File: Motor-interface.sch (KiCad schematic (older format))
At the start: 40 parts, among them J101 0, J102 0, P101 TE-23pins connector, P102 PSU_ISO, P103 Halls, P104 LineContactor, P105 ReverseContactor, P106 FanContactor, P107 Battery+, P108 MC_USB, P109 MC_CAN, P110 HallCurrent, Q101 Q_NPN_BCE, U101 AP1117D50, U102 AP1117D33, U103 TLP2361, U104 TLP2361, U105 TLP2361, U106 TLP2361, U107 TLP2361, U108 TLP2361, U109 Teensy_3.2, U110 TLP2361, U111 FODM3052

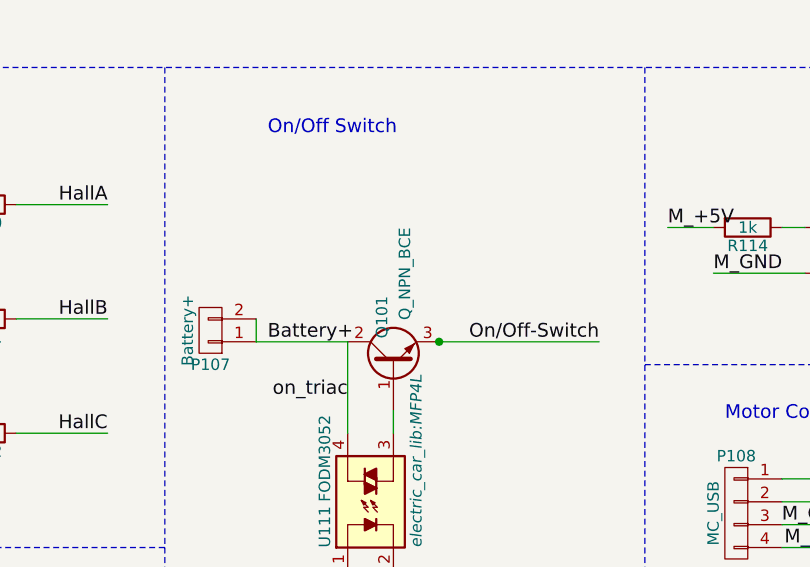
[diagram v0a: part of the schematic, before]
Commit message: renamed transistor (fixed)
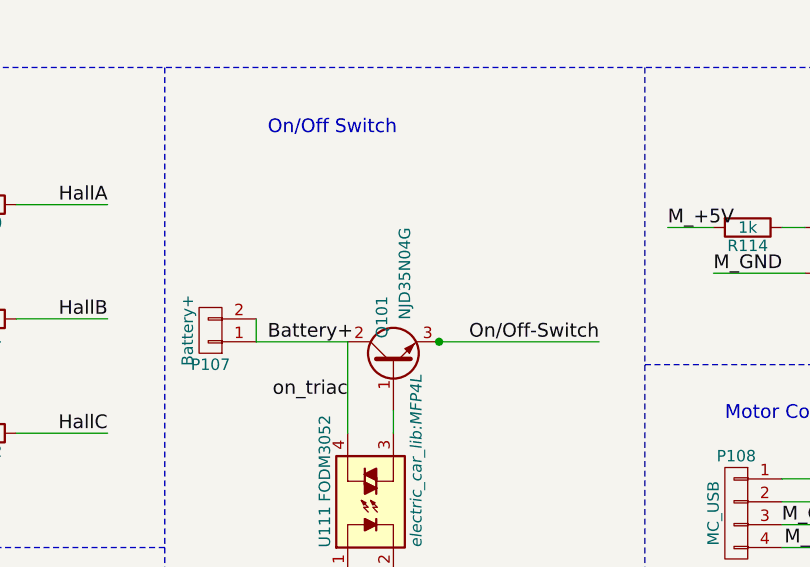
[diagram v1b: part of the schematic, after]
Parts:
- Q101: value Q_NPN_BCE -> NJD35N04G
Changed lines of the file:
@@
 P 7700 4500
 F 0 "Q101" H 8000 4550 50  0000 R CNN
-F 1 "Q_NPN_BCE" H 8300 4450 50  0000 R CNN
+F 1 "NJD35N04G" H 8300 4450 50  0000 R CNN
 F 2 "TO_SOT_Packages_SMD:SOT-428" H 7900 4600 50  0001 C CNN
 F 3 "" H 7700 4500 50  0000 C CNN

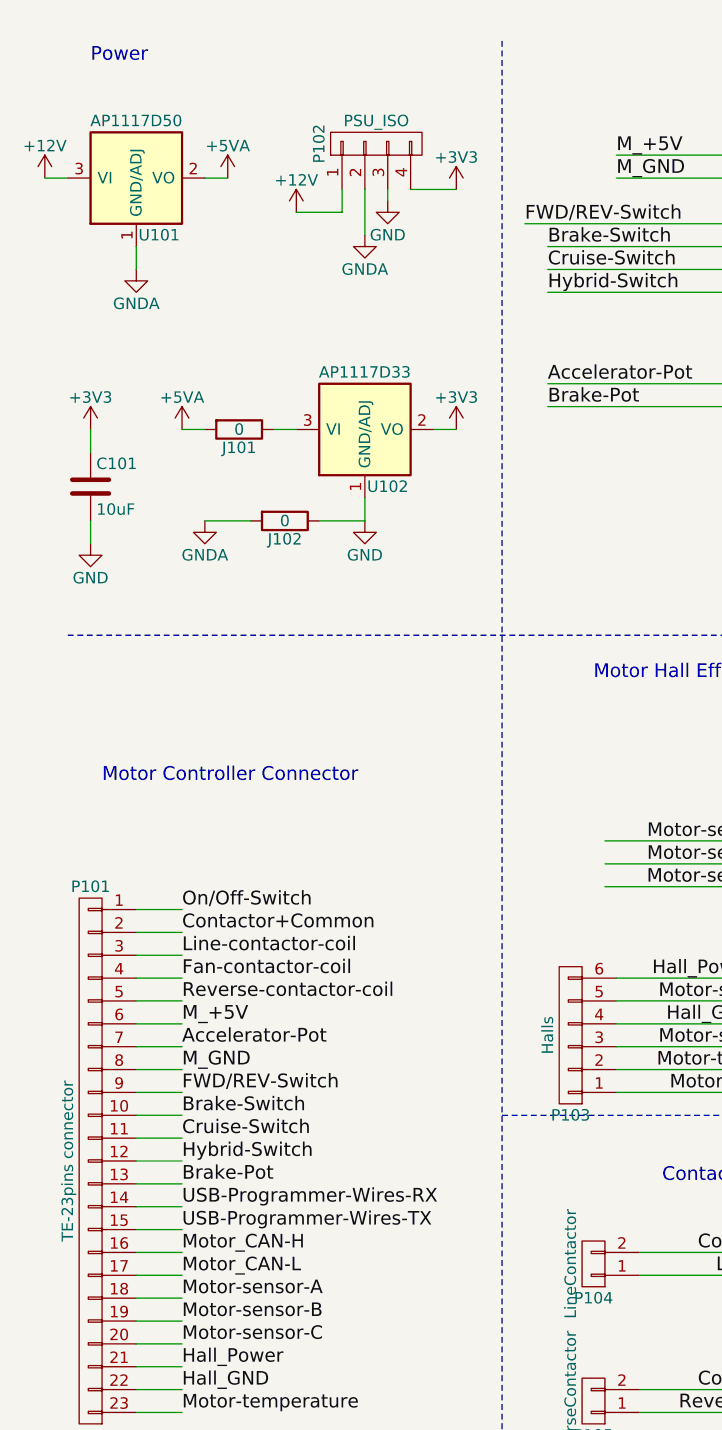
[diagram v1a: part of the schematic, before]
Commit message: pour and silk edits
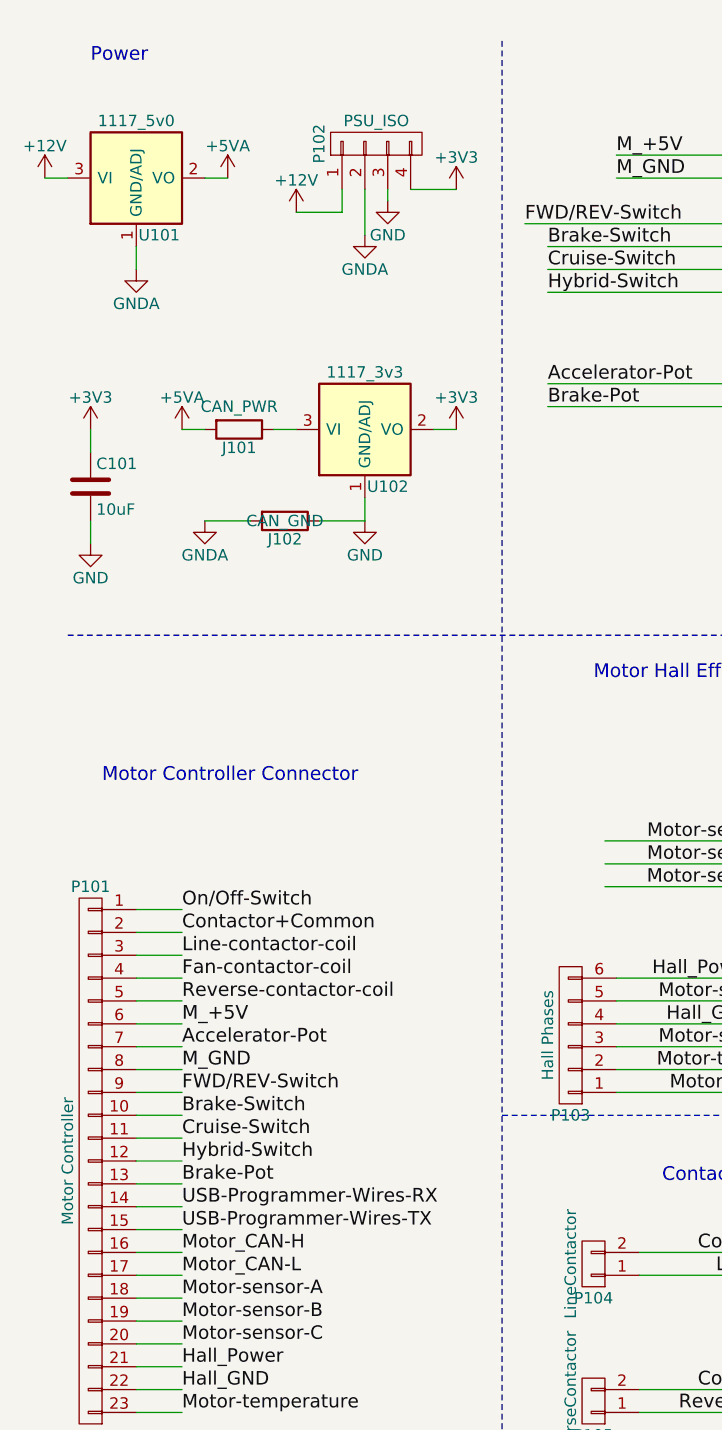
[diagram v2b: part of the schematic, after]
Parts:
- J101: value 0 -> CAN_PWR
- J102: value 0 -> CAN_GND
- P101: value TE-23pins connector -> Motor Controller
- P103: value Halls -> Hall Phases
- U101: value AP1117D50 -> 1117_5v0
- U102: value AP1117D33 -> 1117_3v3
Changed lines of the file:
@@
 P 800 5500
 F 0 "P101" H 800 6700 50  0000 C CNN
-F 1 "TE-23pins connector" V 900 5500 50  0000 C CNN
+F 1 "Motor Controller" V 900 5500 50  0000 C CNN
 F 2 "electric_car_lib:TE_23_pins_776087-1_connector" H 800 5500 50  0001 C CNN
 F 3 "" H 800 5500 50  0000 C CNN
@@
 P 2900 4950
 F 0 "P103" H 2900 5300 50  0000 C CNN
-F 1 "Halls" V 3000 4950 50  0000 C CNN
+F 1 "Hall Phases" V 3000 4950 50  0000 C CNN
 F 2 "Pin_Headers:Pin_Header_Angled_2x03" H 2900 4950 50  0001 C CNN
 F 3 "" H 2900 4950 50  0000 C CNN
@@
 P 2000 2300
 F 0 "U102" H 2100 2050 50  0000 C CNN
-F 1 "AP1117D33" H 2000 2550 50  0000 C CNN
+F 1 "1117_3v3" H 2000 2550 50  0000 C CNN
 F 2 "TO_SOT_Packages_SMD:SOT-223" H 2000 2300 50  0001 C CNN
 F 3 "" H 2000 2300 50  0000 C CNN
@@
 P 1000 1200
 F 0 "U101" H 1100 950 50  0000 C CNN
-F 1 "AP1117D50" H 1000 1450 50  0000 C CNN
+F 1 "1117_5v0" H 1000 1450 50  0000 C CNN
 F 2 "TO_SOT_Packages_SMD:SOT-223" H 1000 1200 50  0001 C CNN
 F 3 "" H 1000 1200 50  0000 C CNN
@@
 P 1650 2700
 F 0 "J102" V 1730 2700 50  0000 C CNN
-F 1 "0" V 1650 2700 50  0000 C CNN
+F 1 "CAN_GND" V 1650 2700 50  0000 C CNN
 F 2 "Resistors_SMD:R_1210_HandSoldering" V 1580 2700 50  0001 C CNN
 F 3 "" H 1650 2700 50  0000 C CNN
@@
 P 1450 2300
 F 0 "J101" V 1530 2300 50  0000 C CNN
-F 1 "0" V 1450 2300 50  0000 C CNN
+F 1 "CAN_PWR" V 1350 2300 50  0000 C CNN
 F 2 "Resistors_SMD:R_1210_HandSoldering" V 1380 2300 50  0001 C CNN
 F 3 "" H 1450 2300 50  0000 C CNN

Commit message: plotted gerbers
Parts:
- added W101, W102: M3, Mounting_Holes:MountingHole_3.5mm_Pad_Via, symbol TEST_1P
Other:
- note added: "Mounting Holes"
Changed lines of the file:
@@
 MOSI
 $Comp
-L GND #PWR01
+L GND #PWR129
 U 1 1 57FCC1C9
 P 7700 5500
-F 0 "#PWR01" H 7700 5250 50  0001 C CNN
+F 0 "#PWR129" H 7700 5250 50  0001 C CNN
 F 1 "GND" H 7700 5350 50  0000 C CNN
 F 2 "" H 7700 5500 50  0000 C CNN
@@
 Motor_CAN-L
 $Comp
-L +3V3 #PWR02
+L +3V3 #PWR128
 U 1 1 582A5D02
 P 7050 1400
-F 0 "#PWR02" H 7050 1250 50  0001 C CNN
+F 0 "#PWR128" H 7050 1250 50  0001 C CNN
 F 1 "+3V3" H 7050 1540 50  0000 C CNN
 F 2 "" H 7050 1400 50  0000 C CNN
@@
 $EndComp
 $Comp
-L GND #PWR03
+L GND #PWR130
 U 1 1 582A5FC1
 P 8850 1200
-F 0 "#PWR03" H 8850 950 50  0001 C CNN
+F 0 "#PWR130" H 8850 950 50  0001 C CNN
 F 1 "GND" H 8850 1050 50  0000 C CNN
 F 2 "" H 8850 1200 50  0000 C CNN
@@
 $EndComp
 $Comp
-L +3V3 #PWR04
+L +3V3 #PWR117
 U 1 1 582BF0B6
 P 5700 5900
-F 0 "#PWR04" H 5700 5750 50  0001 C CNN
+F 0 "#PWR117" H 5700 5750 50  0001 C CNN
 F 1 "+3V3" H 5700 6040 50  0000 C CNN
 F 2 "" H 5700 5900 50  0000 C CNN
@@
 $EndComp
 $Comp
-L +3V3 #PWR05
+L +3V3 #PWR119
 U 1 1 582BF605
 P 5700 6500
-F 0 "#PWR05" H 5700 6350 50  0001 C CNN
+F 0 "#PWR119" H 5700 6350 50  0001 C CNN
 F 1 "+3V3" H 5700 6640 50  0000 C CNN
 F 2 "" H 5700 6500 50  0000 C CNN
@@
 $EndComp
 $Comp
-L +3V3 #PWR06
+L +3V3 #PWR121
 U 1 1 582BF6C1
 P 5700 7100
-F 0 "#PWR06" H 5700 6950 50  0001 C CNN
+F 0 "#PWR121" H 5700 6950 50  0001 C CNN
 F 1 "+3V3" H 5700 7240 50  0000 C CNN
 F 2 "" H 5700 7100 50  0000 C CNN
@@
 $EndComp
 $Comp
-L GND #PWR07
+L GND #PWR118
 U 1 1 582BF99C
 P 5700 6100
-F 0 "#PWR07" H 5700 5850 50  0001 C CNN
+F 0 "#PWR118" H 5700 5850 50  0001 C CNN
 F 1 "GND" H 5700 5950 50  0000 C CNN
 F 2 "" H 5700 6100 50  0000 C CNN
@@
 $EndComp
 $Comp
-L GND #PWR08
+L GND #PWR120
 U 1 1 582BFB0B
 P 5700 6700
-F 0 "#PWR08" H 5700 6450 50  0001 C CNN
+F 0 "#PWR120" H 5700 6450 50  0001 C CNN
 F 1 "GND" H 5700 6550 50  0000 C CNN
 F 2 "" H 5700 6700 50  0000 C CNN
@@
 $EndComp
 $Comp
-L GND #PWR09
+L GND #PWR122
 U 1 1 582BFBC7
 P 5700 7300
-F 0 "#PWR09" H 5700 7050 50  0001 C CNN
+F 0 "#PWR122" H 5700 7050 50  0001 C CNN
 F 1 "GND" H 5700 7150 50  0000 C CNN
 F 2 "" H 5700 7300 50  0000 C CNN
@@
 Connection ~ 4450 4200
 $Comp
-L +3V3 #PWR010
+L +3V3 #PWR123
 U 1 1 582D2C82
 P 5850 3700
-F 0 "#PWR010" H 5850 3550 50  0001 C CNN
+F 0 "#PWR123" H 5850 3550 50  0001 C CNN
 F 1 "+3V3" H 5850 3840 50  0000 C CNN
 F 2 "" H 5850 3700 50  0000 C CNN
@@
 $EndComp
 $Comp
-L +3V3 #PWR011
+L +3V3 #PWR124
 U 1 1 582D2E5B
 P 5850 4200
-F 0 "#PWR011" H 5850 4050 50  0001 C CNN
+F 0 "#PWR124" H 5850 4050 50  0001 C CNN
 F 1 "+3V3" H 5850 4340 50  0000 C CNN
 F 2 "" H 5850 4200 50  0000 C CNN
@@
 $EndComp
 $Comp
-L +3V3 #PWR012
+L +3V3 #PWR125
 U 1 1 582D2F32
 P 5850 4700
-F 0 "#PWR012" H 5850 4550 50  0001 C CNN
+F 0 "#PWR125" H 5850 4550 50  0001 C CNN
 F 1 "+3V3" H 5850 4840 50  0000 C CNN
 F 2 "" H 5850 4700 50  0000 C CNN
@@
 $EndComp
 $Comp
-L GND #PWR013
+L GND #PWR114
 U 1 1 582D31E1
 P 5650 3900
-F 0 "#PWR013" H 5650 3650 50  0001 C CNN
+F 0 "#PWR114" H 5650 3650 50  0001 C CNN
 F 1 "GND" H 5650 3750 50  0000 C CNN
 F 2 "" H 5650 3900 50  0000 C CNN
@@
 $EndComp
 $Comp
-L GND #PWR014
+L GND #PWR115
 U 1 1 582D35E6
 P 5650 4400
-F 0 "#PWR014" H 5650 4150 50  0001 C CNN
+F 0 "#PWR115" H 5650 4150 50  0001 C CNN
 F 1 "GND" H 5650 4250 50  0000 C CNN
 F 2 "" H 5650 4400 50  0000 C CNN
@@
 $EndComp
 $Comp
-L GND #PWR015
+L GND #PWR116
 U 1 1 582D36BD
 P 5650 4900
-F 0 "#PWR015" H 5650 4650 50  0001 C CNN
+F 0 "#PWR116" H 5650 4650 50  0001 C CNN
 F 1 "GND" H 5650 4750 50  0000 C CNN
 F 2 "" H 5650 4900 50  0000 C CNN
@@
 	8900 3900 9100 3900
 $Comp
-L +3V3 #PWR016
+L +3V3 #PWR131
 U 1 1 582D6DBE
 P 10200 3900
-F 0 "#PWR016" H 10200 3750 50  0001 C CNN
+F 0 "#PWR131" H 10200 3750 50  0001 C CNN
 F 1 "+3V3" H 10200 4040 50  0000 C CNN
 F 2 "" H 10200 3900 50  0000 C CNN
@@
 $EndComp
 $Comp
-L GND #PWR017
+L GND #PWR132
 U 1 1 582D6EA4
 P 10200 4100
-F 0 "#PWR017" H 10200 3850 50  0001 C CNN
+F 0 "#PWR132" H 10200 3850 50  0001 C CNN
 F 1 "GND" H 10200 3950 50  0000 C CNN
 F 2 "" H 10200 4100 50  0000 C CNN
@@
 	9400 2200 8700 2200
 $Comp
-L +12V #PWR018
+L +12V #PWR101
 U 1 1 582DCA99
 P 600 1200
-F 0 "#PWR018" H 600 1050 50  0001 C CNN
+F 0 "#PWR101" H 600 1050 50  0001 C CNN
 F 1 "+12V" H 600 1340 50  0000 C CNN
 F 2 "" H 600 1200 50  0000 C CNN
@@
 $EndComp
 $Comp
-L +3V3 #PWR019
+L +3V3 #PWR113
 U 1 1 582DCE09
 P 2400 2300
-F 0 "#PWR019" H 2400 2150 50  0001 C CNN
+F 0 "#PWR113" H 2400 2150 50  0001 C CNN
 F 1 "+3V3" H 2400 2440 50  0000 C CNN
 F 2 "" H 2400 2300 50  0000 C CNN
@@
 $EndComp
 $Comp
-L +5VA #PWR020
+L +5VA #PWR107
 U 1 1 582DCF91
 P 1400 1200
-F 0 "#PWR020" H 1400 1050 50  0001 C CNN
+F 0 "#PWR107" H 1400 1050 50  0001 C CNN
 F 1 "+5VA" H 1400 1340 50  0000 C CNN
 F 2 "" H 1400 1200 50  0000 C CNN
@@
 $EndComp
 $Comp
-L GNDA #PWR021
+L GNDA #PWR104
 U 1 1 582DD099
 P 1000 1600
-F 0 "#PWR021" H 1000 1350 50  0001 C CNN
+F 0 "#PWR104" H 1000 1350 50  0001 C CNN
 F 1 "GNDA" H 1000 1450 50  0000 C CNN
 F 2 "" H 1000 1600 50  0000 C CNN
@@
 $EndComp
 $Comp
-L GND #PWR022
+L GND #PWR110
 U 1 1 582DD15D
 P 2000 2700
-F 0 "#PWR022" H 2000 2450 50  0001 C CNN
+F 0 "#PWR110" H 2000 2450 50  0001 C CNN
 F 1 "GND" H 2000 2550 50  0000 C CNN
 F 2 "" H 2000 2700 50  0000 C CNN
@@
 	2400 2300 2300 2300
 $Comp
-L +5VA #PWR023
+L +5VA #PWR105
 U 1 1 582E256C
 P 1200 2300
-F 0 "#PWR023" H 1200 2150 50  0001 C CNN
+F 0 "#PWR105" H 1200 2150 50  0001 C CNN
 F 1 "+5VA" H 1200 2440 50  0000 C CNN
 F 2 "" H 1200 2300 50  0000 C CNN
@@
 $EndComp
 $Comp
-L GNDA #PWR024
+L GNDA #PWR106
 U 1 1 582E2A4A
 P 1300 2700
-F 0 "#PWR024" H 1300 2450 50  0001 C CNN
+F 0 "#PWR106" H 1300 2450 50  0001 C CNN
 F 1 "GNDA" H 1300 2550 50  0000 C CNN
 F 2 "" H 1300 2700 50  0000 C CNN
@@
 $EndComp
 $Comp
-L GNDA #PWR025
+L GNDA #PWR109
 U 1 1 582E4970
 P 2000 1450
-F 0 "#PWR025" H 2000 1200 50  0001 C CNN
+F 0 "#PWR109" H 2000 1200 50  0001 C CNN
 F 1 "GNDA" H 2000 1300 50  0000 C CNN
 F 2 "" H 2000 1450 50  0000 C CNN
@@
 $EndComp
 $Comp
-L GND #PWR026
+L GND #PWR111
 U 1 1 582E4EF7
 P 2100 1300
-F 0 "#PWR026" H 2100 1050 50  0001 C CNN
+F 0 "#PWR111" H 2100 1050 50  0001 C CNN
 F 1 "GND" H 2100 1150 50  0000 C CNN
 F 2 "" H 2100 1300 50  0000 C CNN
@@
 $EndComp
 $Comp
-L +3V3 #PWR027
+L +3V3 #PWR112
 U 1 1 582E4FE6
 P 2400 1250
-F 0 "#PWR027" H 2400 1100 50  0001 C CNN
+F 0 "#PWR112" H 2400 1100 50  0001 C CNN
 F 1 "+3V3" H 2400 1390 50  0000 C CNN
 F 2 "" H 2400 1250 50  0000 C CNN
@@
 $EndComp
 $Comp
-L +12V #PWR028
+L +12V #PWR108
 U 1 1 582E50D5
 P 1700 1350
-F 0 "#PWR028" H 1700 1200 50  0001 C CNN
+F 0 "#PWR108" H 1700 1200 50  0001 C CNN
 F 1 "+12V" H 1700 1490 50  0000 C CNN
 F 2 "" H 1700 1350 50  0000 C CNN
@@
 $EndComp
 $Comp
-L +3V3 #PWR029
+L +3V3 #PWR102
 U 1 1 582E74E8
 P 800 2300
-F 0 "#PWR029" H 800 2150 50  0001 C CNN
+F 0 "#PWR102" H 800 2150 50  0001 C CNN
 F 1 "+3V3" H 800 2440 50  0000 C CNN
 F 2 "" H 800 2300 50  0000 C CNN
@@
 $EndComp
 $Comp
-L GND #PWR030
+L GND #PWR103
 U 1 1 582E75D7
 P 800 2800
-F 0 "#PWR030" H 800 2550 50  0001 C CNN
+F 0 "#PWR103" H 800 2550 50  0001 C CNN
 F 1 "GND" H 800 2650 50  0000 C CNN
 F 2 "" H 800 2800 50  0000 C CNN
@@
 $EndComp
 $Comp
-L +3V3 #PWR031
+L +3V3 #PWR126
 U 1 1 582D980D
 P 6300 1300
-F 0 "#PWR031" H 6300 1150 50  0001 C CNN
+F 0 "#PWR126" H 6300 1150 50  0001 C CNN
 F 1 "+3V3" H 6300 1440 50  0000 C CNN
 F 2 "" H 6300 1300 50  0000 C CNN
@@
 $EndComp
 $Comp
-L GND #PWR032
+L GND #PWR127
 U 1 1 582D98FC
 P 6550 1250
-F 0 "#PWR032" H 6550 1000 50  0001 C CNN
+F 0 "#PWR127" H 6550 1000 50  0001 C CNN
 F 1 "GND" H 6550 1100 50  0000 C CNN
 F 2 "" H 6550 1250 50  0000 C CNN
@@
 Wire Wire Line
 	7500 4400 7500 4800
+$Comp
+L TEST_1P W101
+U 1 1 582D571F
+P 1100 7400
+F 0 "W101" H 1100 7670 50  0000 C CNN
+F 1 "M3" H 1100 7600 50  0000 C CNN
+F 2 "Mounting_Holes:MountingHole_3.5mm_Pad_Via" H 1300 7400 50  0001 C CNN
+F 3 "" H 1300 7400 50  0000 C CNN
+	1    1100 7400
+	1    0    0    -1
+$EndComp
+$Comp
+L TEST_1P W102
+U 1 1 582D5A90
+P 1500 7400
+F 0 "W102" H 1500 7670 50  0000 C CNN
+F 1 "M3" H 1500 7600 50  0000 C CNN
+F 2 "Mounting_Holes:MountingHole_3.5mm_Pad_Via" H 1700 7400 50  0001 C CNN
+F 3 "" H 1700 7400 50  0000 C CNN
+	1    1500 7400
+	1    0    0    -1
+$EndComp
+Text Notes 1000 7600 0    60   ~ 0
+Mounting Holes
 $EndSCHEMATC
